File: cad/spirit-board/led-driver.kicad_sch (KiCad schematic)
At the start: 63 parts, among them J10 H COIL, J11 I COIL, J12 J COIL, J13 K COIL, J14 L COIL, J15 M COIL, J16 N COIL, J17 O COIL, J18 P COIL, J19 Q COIL, J20 Y COIL, J21 R COIL, J22 Z COIL, J23 S COIL, J24 0 COIL, J25 T COIL, J26 1 COIL, J27 U COIL, J28 2 COIL, J29 V COIL, J3 A COIL, J30 3 COIL, J31 W COIL, J32 4 COIL, J33 X COIL, J34 5 COIL, J35 6 COIL, J37 7 COIL, J39 8 COIL, J4 B COIL, J41 9 COIL, J5 C COIL, J6 D COIL, J7 E COIL, J8 F COIL, J9 G COIL, U1 TLC59401PWP, U2 TLC59401PWP, U3 TLC59401PWP

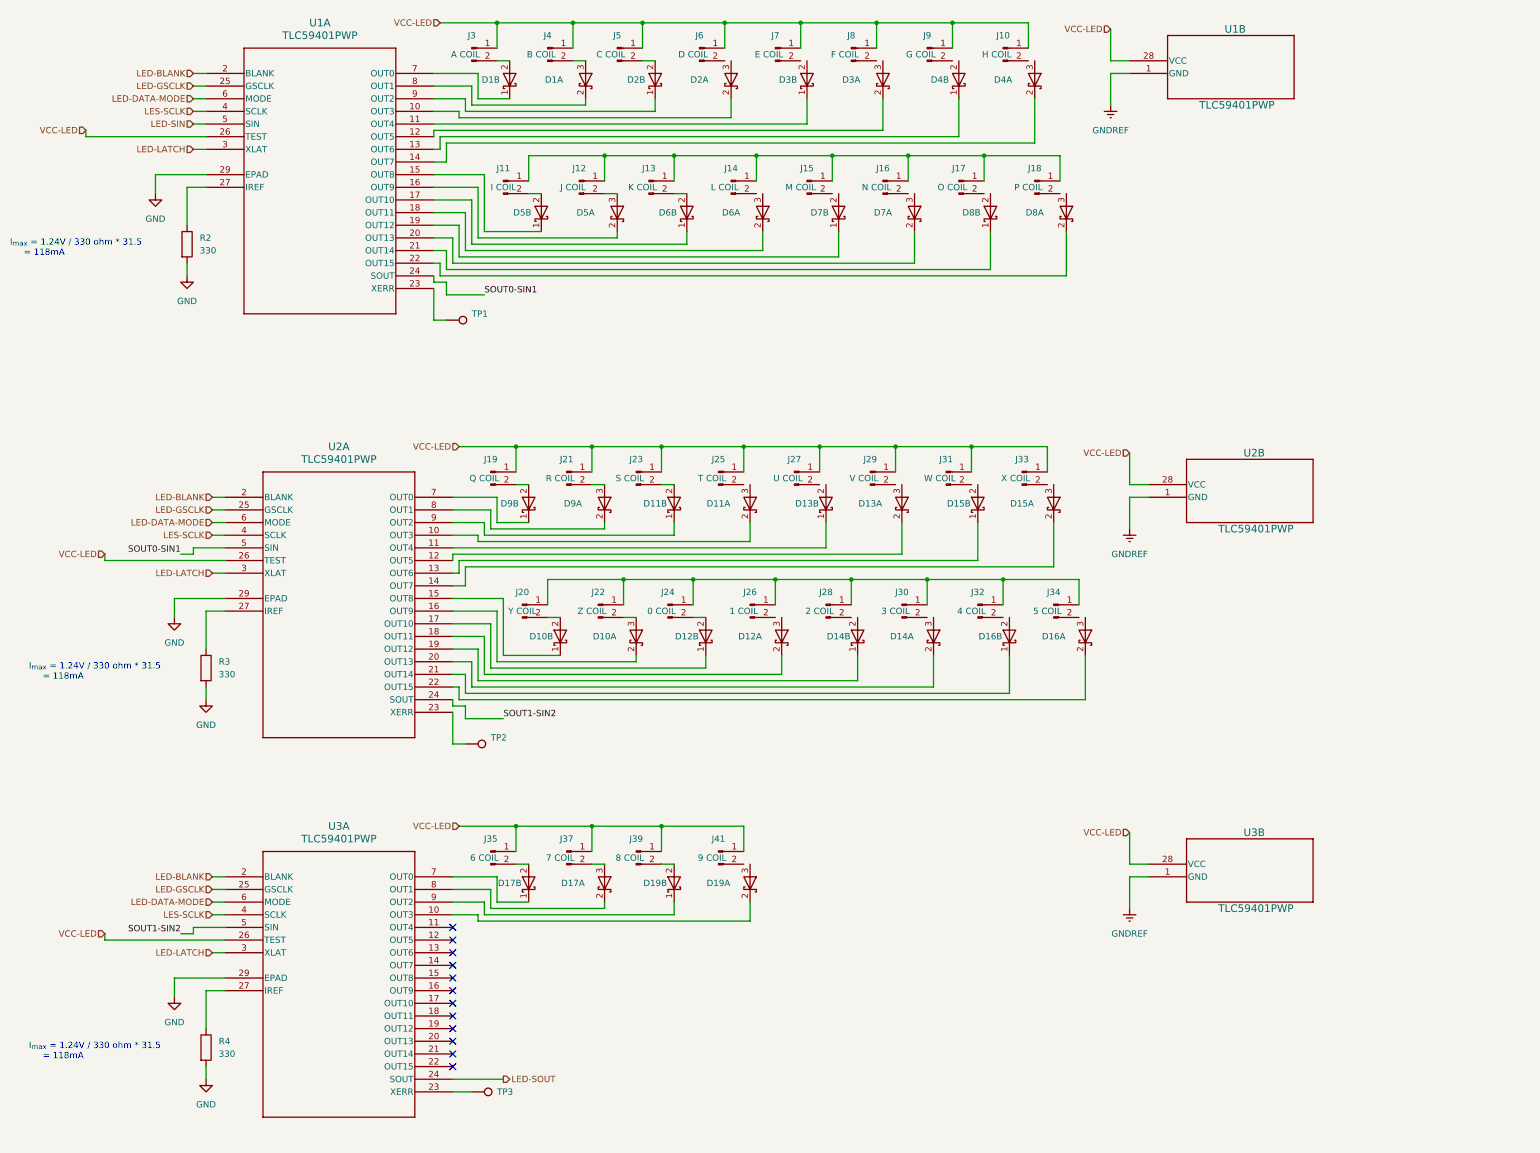
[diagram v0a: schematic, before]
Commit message: Mike's feedback
 - bypass caps on all power sources
 - Bulk cap on LED power
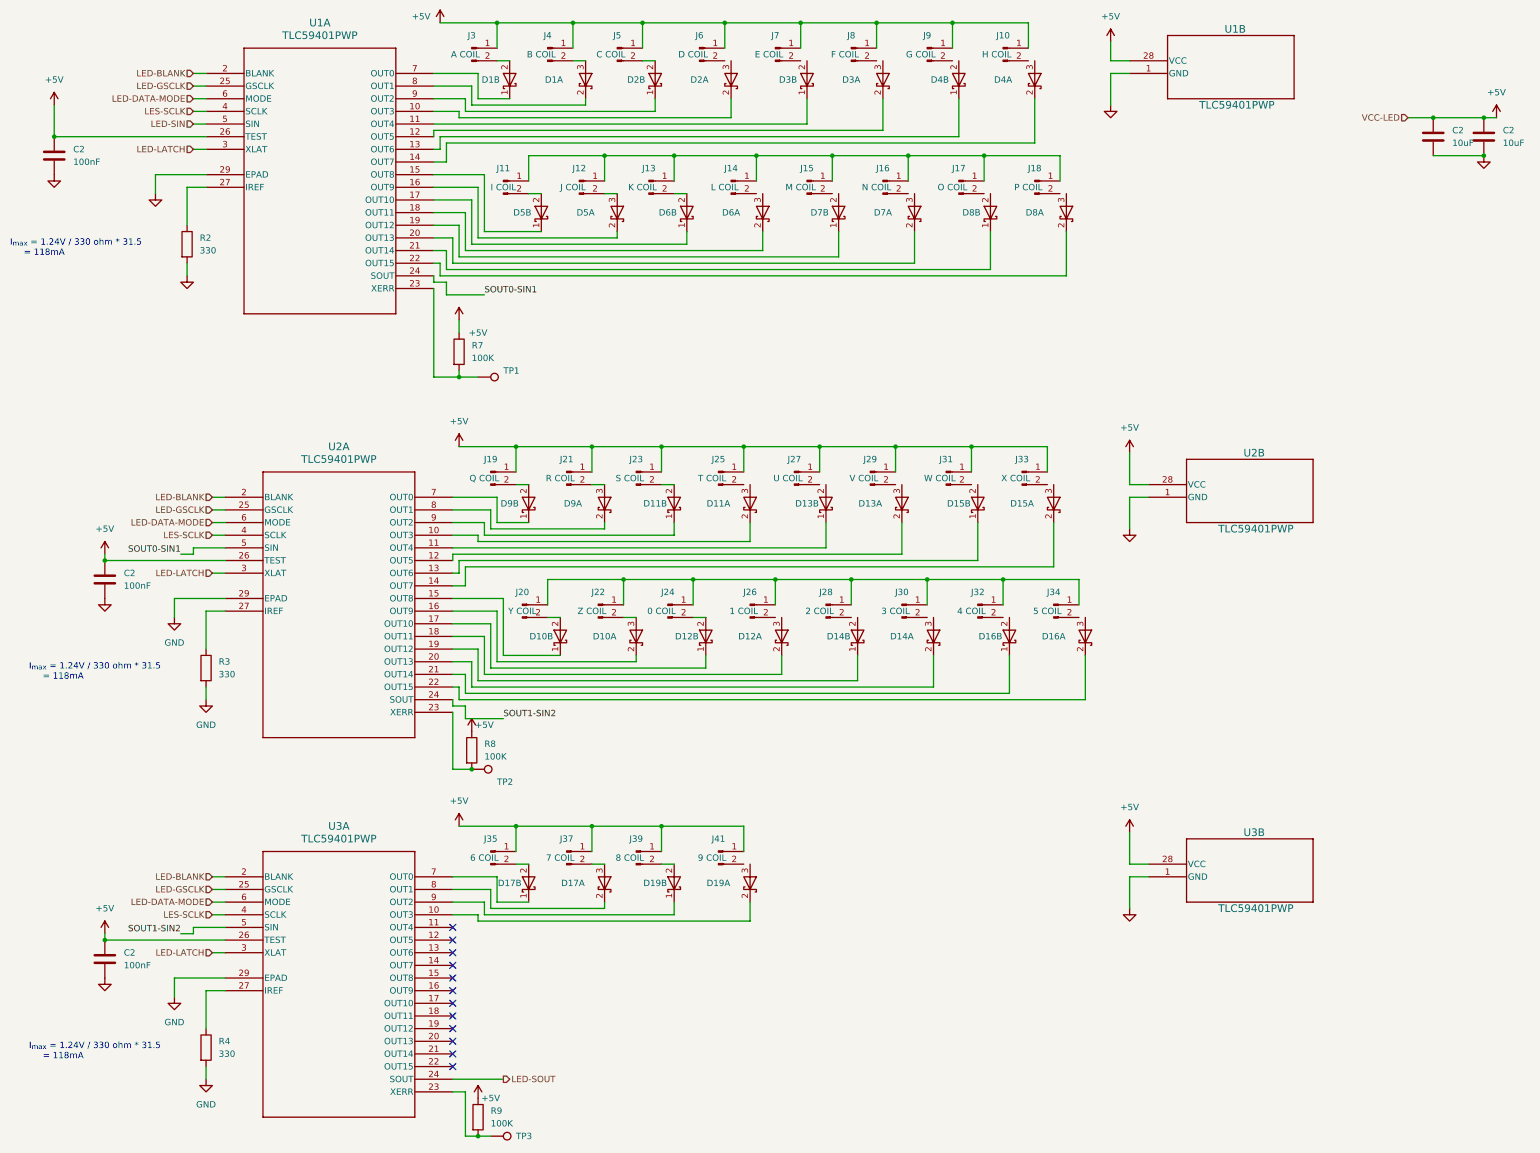
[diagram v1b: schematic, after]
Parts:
- added C2 (x3): 100nF, symbol Device:C
- added C2 (x2): 10uF, symbol Device:C
- added R7, R8, R9: 100K, symbol Device:R
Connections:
- net GNDREF is gone; now on net GND: U1.1 (GND), U2.1 (GND), U3.1 (GND)
- net GND: now also C2.2, C2.2, C2.2, C2.2, C2.2
- net at TP3.1, U3.23 (XERR): now also R9.2
- net at TP1.1, U1.23 (XERR): now also R7.2
- net at TP2.1, U2.23 (XERR): now also R8.2
- net VCC-LED renamed +5V
- net +5V: now also C2.1, C2.1, C2.1, C2.1, C2.1, R7.1, R8.1, R9.1
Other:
- moved on the sheet: TP1, TP2, TP3

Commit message: per-coil schematic
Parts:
- removed C2 (x3): 100nF, symbol Device:C
- removed D1, D10, D11, D12, D13, D14, D15, D16, D17, D19, D2, D3, D4, D5, D6, D7, D8, D9: D_Schottky_Dual_Series_KCA_Split, symbol Device:D_Schottky_Dual_Series_KCA_Split
- removed J10: H COIL, symbol Connector:Conn_01x02_Pin
- removed J11: I COIL, symbol Connector:Conn_01x02_Pin
- removed J12: J COIL, symbol Connector:Conn_01x02_Pin
- removed J13: K COIL, symbol Connector:Conn_01x02_Pin
- removed J14: L COIL, symbol Connector:Conn_01x02_Pin
- removed J15: M COIL, symbol Connector:Conn_01x02_Pin
- removed J16: N COIL, symbol Connector:Conn_01x02_Pin
- removed J17: O COIL, symbol Connector:Conn_01x02_Pin
- removed J18: P COIL, symbol Connector:Conn_01x02_Pin
- removed J19: Q COIL, symbol Connector:Conn_01x02_Pin
- removed J20: Y COIL, symbol Connector:Conn_01x02_Pin
- removed J21: R COIL, symbol Connector:Conn_01x02_Pin
- removed J22: Z COIL, symbol Connector:Conn_01x02_Pin
- removed J23: S COIL, symbol Connector:Conn_01x02_Pin
- removed J24: 0 COIL, symbol Connector:Conn_01x02_Pin
- removed J25: T COIL, symbol Connector:Conn_01x02_Pin
- removed J26: 1 COIL, symbol Connector:Conn_01x02_Pin
- removed J27: U COIL, symbol Connector:Conn_01x02_Pin
- removed J28: 2 COIL, symbol Connector:Conn_01x02_Pin
- removed J29: V COIL, symbol Connector:Conn_01x02_Pin
- removed J3: A COIL, symbol Connector:Conn_01x02_Pin
- removed J30: 3 COIL, symbol Connector:Conn_01x02_Pin
- removed J31: W COIL, symbol Connector:Conn_01x02_Pin
- removed J32: 4 COIL, symbol Connector:Conn_01x02_Pin
- removed J33: X COIL, symbol Connector:Conn_01x02_Pin
- removed J34: 5 COIL, symbol Connector:Conn_01x02_Pin
- removed J35: 6 COIL, symbol Connector:Conn_01x02_Pin
- removed J37: 7 COIL, symbol Connector:Conn_01x02_Pin
- removed J39: 8 COIL, symbol Connector:Conn_01x02_Pin
- removed J4: B COIL, symbol Connector:Conn_01x02_Pin
- removed J41: 9 COIL, symbol Connector:Conn_01x02_Pin
- removed J5: C COIL, symbol Connector:Conn_01x02_Pin
- removed J6: D COIL, symbol Connector:Conn_01x02_Pin
- removed J7: E COIL, symbol Connector:Conn_01x02_Pin
- removed J8: F COIL, symbol Connector:Conn_01x02_Pin
- removed J9: G COIL, symbol Connector:Conn_01x02_Pin
- added C2 (x3): 100nF, symbol Device:C
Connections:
- net +5V: now also C2.1, C2.1, C2.1
- net GND: now also C2.2, C2.2, C2.2
- net 9-COIL/L: now reaches U3.10 (OUT3)
- net X-COIL/L: now reaches U2.14 (OUT7)
- net O-COIL/L: now reaches U1.21 (OUT14)
- net Y-COIL/L: now reaches U2.15 (OUT8)
- net B-COIL/L: now reaches U1.8 (OUT1)
- net A-COIL/L: now reaches U1.7 (OUT0)
- net 0-COIL/L: now reaches U2.17 (OUT10)
- net 3-COIL/L: now reaches U2.20 (OUT13)
- net U-COIL/L: now reaches U2.11 (OUT4)
- net N-COIL/L: now reaches U1.20 (OUT13)
- net D-COIL/L: now reaches U1.10 (OUT3)
- net L-COIL/L: now reaches U1.18 (OUT11)
- net Z-COIL/L: now reaches U2.16 (OUT9)
- net J-COIL/L: now reaches U1.16 (OUT9)
- net R-COIL/L: now reaches U2.8 (OUT1)
- net M-COIL/L: now reaches U1.19 (OUT12)
- net E-COIL/L: now reaches U1.11 (OUT4)
- net YES-COIL/L: now reaches U3.11 (OUT4)
- net NO-COIL/L: now reaches U3.12 (OUT5)
- net 6-COIL/L: now reaches U3.7 (OUT0)
- net 7-COIL/L: now reaches U3.8 (OUT1)
- net 8-COIL/L: now reaches U3.9 (OUT2)
- net G-COIL/L: now reaches U1.13 (OUT6)
- net I-COIL/L: now reaches U1.15 (OUT8)
- net 5-COIL/L: now reaches U2.22 (OUT15)
- net H-COIL/L: now reaches U1.14 (OUT7)
- net F-COIL/L: now reaches U1.12 (OUT5)
- net K-COIL/L: now reaches U1.17 (OUT10)
- net P-COIL/L: now reaches U1.22 (OUT15)
- net C-COIL/L: now reaches U1.9 (OUT2)
- net W-COIL/L: now reaches U2.13 (OUT6)
- net 2-COIL/L: now reaches U2.19 (OUT12)
- net 4-COIL/L: now reaches U2.21 (OUT14)
- net S-COIL/L: now reaches U2.9 (OUT2)
- net V-COIL/L: now reaches U2.12 (OUT5)
- net Q-COIL/L: now reaches U2.7 (OUT0)
- net T-COIL/L: now reaches U2.10 (OUT3)
- net 1-COIL/L: now reaches U2.18 (OUT11)
- no-connect marks 12 -> 10
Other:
- added sheet 0-COIL (coil.kicad_sch)
- added sheet 1-COIL (coil.kicad_sch)
- added sheet 2-COIL (coil.kicad_sch)
- added sheet 3-COIL (coil.kicad_sch)
- added sheet 4-COIL (coil.kicad_sch)
- added sheet 5-COIL (coil.kicad_sch)
- added sheet 6-COIL (coil.kicad_sch)
- added sheet 7-COIL (coil.kicad_sch)
- added sheet 8-COIL (coil.kicad_sch)
- added sheet 9-COIL (coil.kicad_sch)
- added sheet A-COIL (coil.kicad_sch)
- added sheet B-COIL (coil.kicad_sch)
- added sheet C-COIL (coil.kicad_sch)
- added sheet D-COIL (coil.kicad_sch)
- added sheet E-COIL (coil.kicad_sch)
- added sheet F-COIL (coil.kicad_sch)
- added sheet G-COIL (coil.kicad_sch)
- added sheet H-COIL (coil.kicad_sch)
- added sheet I-COIL (coil.kicad_sch)
- added sheet J-COIL (coil.kicad_sch)
- added sheet K-COIL (coil.kicad_sch)
- added sheet L-COIL (coil.kicad_sch)
- added sheet M-COIL (coil.kicad_sch)
- added sheet N-COIL (coil.kicad_sch)
- added sheet NO-COIL (coil.kicad_sch)
- added sheet O-COIL (coil.kicad_sch)
- added sheet P-COIL (coil.kicad_sch)
- added sheet Q-COIL (coil.kicad_sch)
- added sheet R-COIL (coil.kicad_sch)
- added sheet S-COIL (coil.kicad_sch)
- added sheet T-COIL (coil.kicad_sch)
- added sheet U-COIL (coil.kicad_sch)
- added sheet V-COIL (coil.kicad_sch)
- added sheet W-COIL (coil.kicad_sch)
- added sheet X-COIL (coil.kicad_sch)
- added sheet Y-COIL (coil.kicad_sch)
- added sheet YES-COIL (coil.kicad_sch)
- added sheet Z-COIL (coil.kicad_sch)
- moved on the sheet: U1B, U2B
